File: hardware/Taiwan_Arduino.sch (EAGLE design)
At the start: 46 parts, among them J1 AVR_SPI_PRG_62X3_LOCK, T1 2SC, T2 2N, U1 ATMEGA328P_PDIP

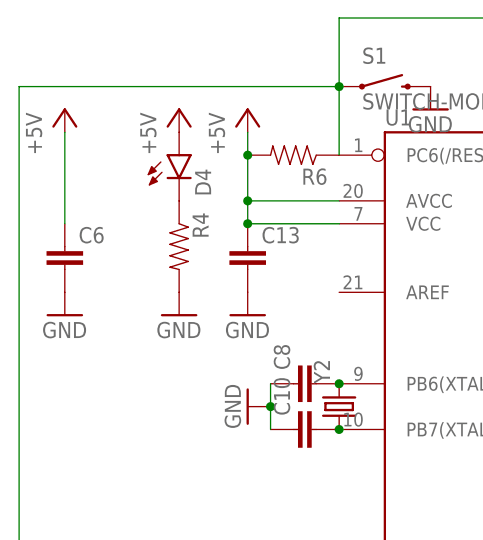
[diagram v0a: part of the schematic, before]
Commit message: Replaace bypass cap
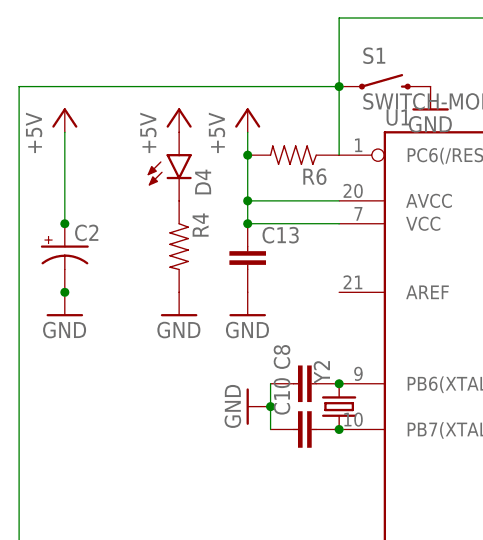
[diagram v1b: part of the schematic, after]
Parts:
- removed C6: (no value), SparkFun-Capacitors:CAPPTH1
- added C2: (no value), SparkFun-Capacitors:CAP_POLPTH1
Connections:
- net +5V: now also C2.+; no longer C6.1
- net GND: now also C2.-; no longer C6.2
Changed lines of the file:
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@@
 <grid distance="0.1" unitdist="inch" unit="inch" style="lines" multiple="1" display="no" altdistance="0.01" altunitdist="inch" altunit="inch"/>
 <layers>
-<layer number="1" name="Top" color="4" fill="1" visible="yes" active="no"/>
-<layer number="16" name="Bottom" color="1" fill="1" visible="yes" active="no"/>
-<layer number="17" name="Pads" color="2" fill="1" visible="yes" active="no"/>
-<layer number="18" name="Vias" color="2" fill="1" visible="yes" active="no"/>
-<layer number="19" name="Unrouted" color="6" fill="1" visible="yes" active="no"/>
-<layer number="20" name="Dimension" color="15" fill="1" visible="yes" active="no"/>
-<layer number="21" name="tPlace" color="7" fill="1" visible="yes" active="no"/>
-<layer number="22" name="bPlace" color="7" fill="1" visible="yes" active="no"/>
-<layer number="23" name="tOrigins" color="15" fill="1" visible="yes" active="no"/>
-<layer number="24" name="bOrigins" color="15" fill="1" visible="yes" active="no"/>
-<layer number="25" name="tNames" color="7" fill="1" visible="yes" active="no"/>
-<layer number="26" name="bNames" color="7" fill="1" visible="yes" active="no"/>
-<layer number="27" name="tValues" color="7" fill="1" visible="yes" active="no"/>
-<layer number="28" name="bValues" color="7" fill="1" visible="yes" active="no"/>
+<layer number="1" name="Top" color="4" fill="1" visible="no" active="no"/>
+<layer number="16" name="Bottom" color="1" fill="1" visible="no" active="no"/>
+<layer number="17" name="Pads" color="2" fill="1" visible="no" active="no"/>
+<layer number="18" name="Vias" color="2" fill="1" visible="no" active="no"/>
+<layer number="19" name="Unrouted" color="6" fill="1" visible="no" active="no"/>
+<layer number="20" name="Dimension" color="15" fill="1" visible="no" active="no"/>
+<layer number="21" name="tPlace" color="7" fill="1" visible="no" active="no"/>
+<layer number="22" name="bPlace" color="7" fill="1" visible="no" active="no"/>
+<layer number="23" name="tOrigins" color="15" fill="1" visible="no" active="no"/>
+<layer number="24" name="bOrigins" color="15" fill="1" visible="no" active="no"/>
+<layer number="25" name="tNames" color="7" fill="1" visible="no" active="no"/>
+<layer number="26" name="bNames" color="7" fill="1" visible="no" active="no"/>
+<layer number="27" name="tValues" color="7" fill="1" visible="no" active="no"/>
+<layer number="28" name="bValues" color="7" fill="1" visible="no" active="no"/>
 <layer number="29" name="tStop" color="7" fill="3" visible="no" active="no"/>
 <layer number="30" name="bStop" color="7" fill="6" visible="no" active="no"/>
@@
 <layer number="35" name="tGlue" color="7" fill="4" visible="no" active="no"/>
 <layer number="36" name="bGlue" color="7" fill="5" visible="no" active="no"/>
-<layer number="37" name="tTest" color="7" fill="1" visible="yes" active="no"/>
-<layer number="38" name="bTest" color="7" fill="1" visible="yes" active="no"/>
+<layer number="37" name="tTest" color="7" fill="1" visible="no" active="no"/>
+<layer number="38" name="bTest" color="7" fill="1" visible="no" active="no"/>
 <layer number="39" name="tKeepout" color="4" fill="11" visible="no" active="no"/>
 <layer number="40" name="bKeepout" color="1" fill="11" visible="no" active="no"/>
@@
 <layer number="44" name="Drills" color="7" fill="1" visible="no" active="no"/>
 <layer number="45" name="Holes" color="7" fill="1" visible="no" active="no"/>
-<layer number="46" name="Milling" color="3" fill="1" visible="yes" active="no"/>
-<layer number="47" name="Measures" color="7" fill="1" visible="yes" active="no"/>
-<layer number="48" name="Document" color="7" fill="1" visible="yes" active="no"/>
-<layer number="49" name="Reference" color="7" fill="1" visible="yes" active="no"/>
-<layer number="50" name="dxf" color="7" fill="1" visible="yes" active="no"/>
-<layer number="51" name="tDocu" color="7" fill="1" visible="yes" active="no"/>
-<layer number="52" name="bDocu" color="7" fill="1" visible="yes" active="no"/>
-<layer number="53" name="tGND_GNDA" color="7" fill="9" visible="yes" active="no"/>
-<layer number="54" name="bGND_GNDA" color="1" fill="9" visible="yes" active="no"/>
-<layer number="56" name="wert" color="7" fill="1" visible="yes" active="no"/>
-<layer number="57" name="tCAD" color="7" fill="1" visible="yes" active="no"/>
-<layer number="59" name="tCarbon" color="7" fill="1" visible="yes" active="no"/>
-<layer number="60" name="bCarbon" color="7" fill="1" visible="yes" active="no"/>
+<layer number="46" name="Milling" color="3" fill="1" visible="no" active="no"/>
+<layer number="47" name="Measures" color="7" fill="1" visible="no" active="no"/>
+<layer number="48" name="Document" color="7" fill="1" visible="no" active="no"/>
+<layer number="49" name="Reference" color="7" fill="1" visible="no" active="no"/>
+<layer number="50" name="dxf" color="7" fill="1" visible="no" active="no"/>
+<layer number="51" name="tDocu" color="7" fill="1" visible="no" active="no"/>
+<layer number="52" name="bDocu" color="7" fill="1" visible="no" active="no"/>
+<layer number="53" name="tGND_GNDA" color="7" fill="9" visible="no" active="no"/>
+<layer number="54" name="bGND_GNDA" color="1" fill="9" visible="no" active="no"/>
+<layer number="56" name="wert" color="7" fill="1" visible="no" active="no"/>
+<layer number="57" name="tCAD" color="7" fill="1" visible="no" active="no"/>
+<layer number="59" name="tCarbon" color="7" fill="1" visible="no" active="no"/>
+<layer number="60" name="bCarbon" color="7" fill="1" visible="no" active="no"/>
 <layer number="90" name="Modules" color="5" fill="1" visible="yes" active="yes"/>
 <layer number="91" name="Nets" color="2" fill="1" visible="yes" active="yes"/>
@@
 <part name="R17" library="SparkFun-Resistors" deviceset="RESISTOR" device="PTH-1/4W-VERT"/>
 <part name="P+8" library="supply1" deviceset="+5V" device=""/>
-<part name="C6" library="SparkFun-Capacitors" deviceset="CAP" device="PTH1"/>
 <part name="GND18" library="supply1" deviceset="GND" device=""/>
 <part name="T1" library="transistor" deviceset="2SC1815" device="" value="2SC"/>
 <part name="T2" library="adafruit" deviceset="2N2222" device="" value="2N"/>
+<part name="C2" library="SparkFun-Capacitors" deviceset="CAP_POL" device="PTH1"/>
 </parts>
 <sheets>
@@
 <instance part="R17" gate="G$1" x="109.22" y="86.36" rot="R270"/>
 <instance part="P+8" gate="1" x="7.62" y="137.16"/>
-<instance part="C6" gate="G$1" x="7.62" y="119.38"/>
 <instance part="GND18" gate="1" x="7.62" y="114.3"/>
 <instance part="T1" gate="G$1" x="160.02" y="83.82"/>
 <instance part="T2" gate="G$1" x="152.4" y="83.82"/>
+<instance part="C2" gate="G$1" x="7.62" y="121.92"/>
 </instances>
 <busses>
@@
 </segment>
 <segment>
-<pinref part="C6" gate="G$1" pin="2"/>
-<pinref part="GND18" gate="1" pin="GND"/>
-</segment>
-<segment>
 <pinref part="T1" gate="G$1" pin="E"/>
 <wire x1="154.94" y1="78.74" x2="162.56" y2="78.74" width="0.1524" layer="91"/>
@@
 <pinref part="T2" gate="G$1" pin="E"/>
 <junction x="162.56" y="78.74"/>
+</segment>
+<segment>
+<pinref part="GND18" gate="1" pin="GND"/>
+<pinref part="C2" gate="G$1" pin="-"/>
+<junction x="7.62" y="116.84"/>
+<pinref part="C2" gate="G$1" pin="-"/>
 </segment>
 </net>
@@
 </segment>
 <segment>
-<pinref part="C6" gate="G$1" pin="1"/>
 <wire x1="7.62" y1="134.62" x2="7.62" y2="124.46" width="0.1524" layer="91"/>
 <pinref part="P+8" gate="1" pin="+5V"/>
-</segment>
-<segment>
+<pinref part="C2" gate="G$1" pin="+"/>
+<junction x="7.62" y="124.46"/>
+</segment>
+<segment>

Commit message: Layout fixed
1.reduce via under the 328p mcu
2.fix the reset pin routing of the isp header
3.beef up the power/ground wires near C13 / reset button and USB shell
4.rotate the speaker header and transistors 45 deg
5.make more space for capacitor C1/C2
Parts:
- removed C3: (no value), SparkFun-Capacitors:CAPPTH1
- added C1: (no value), adafruit:CPOL-USE2.5-5
- C2: device SparkFun-Capacitors:CAP_POLPTH1 -> adafruit:CPOL-USE5-10.5
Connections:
- removed net N$30: C3.2, JP3.2
- net +5V: now also C1.+
- net GND: now also C1.-
- net N$18: now also JP3.2; no longer C3.1
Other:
- moved on the sheet: C2

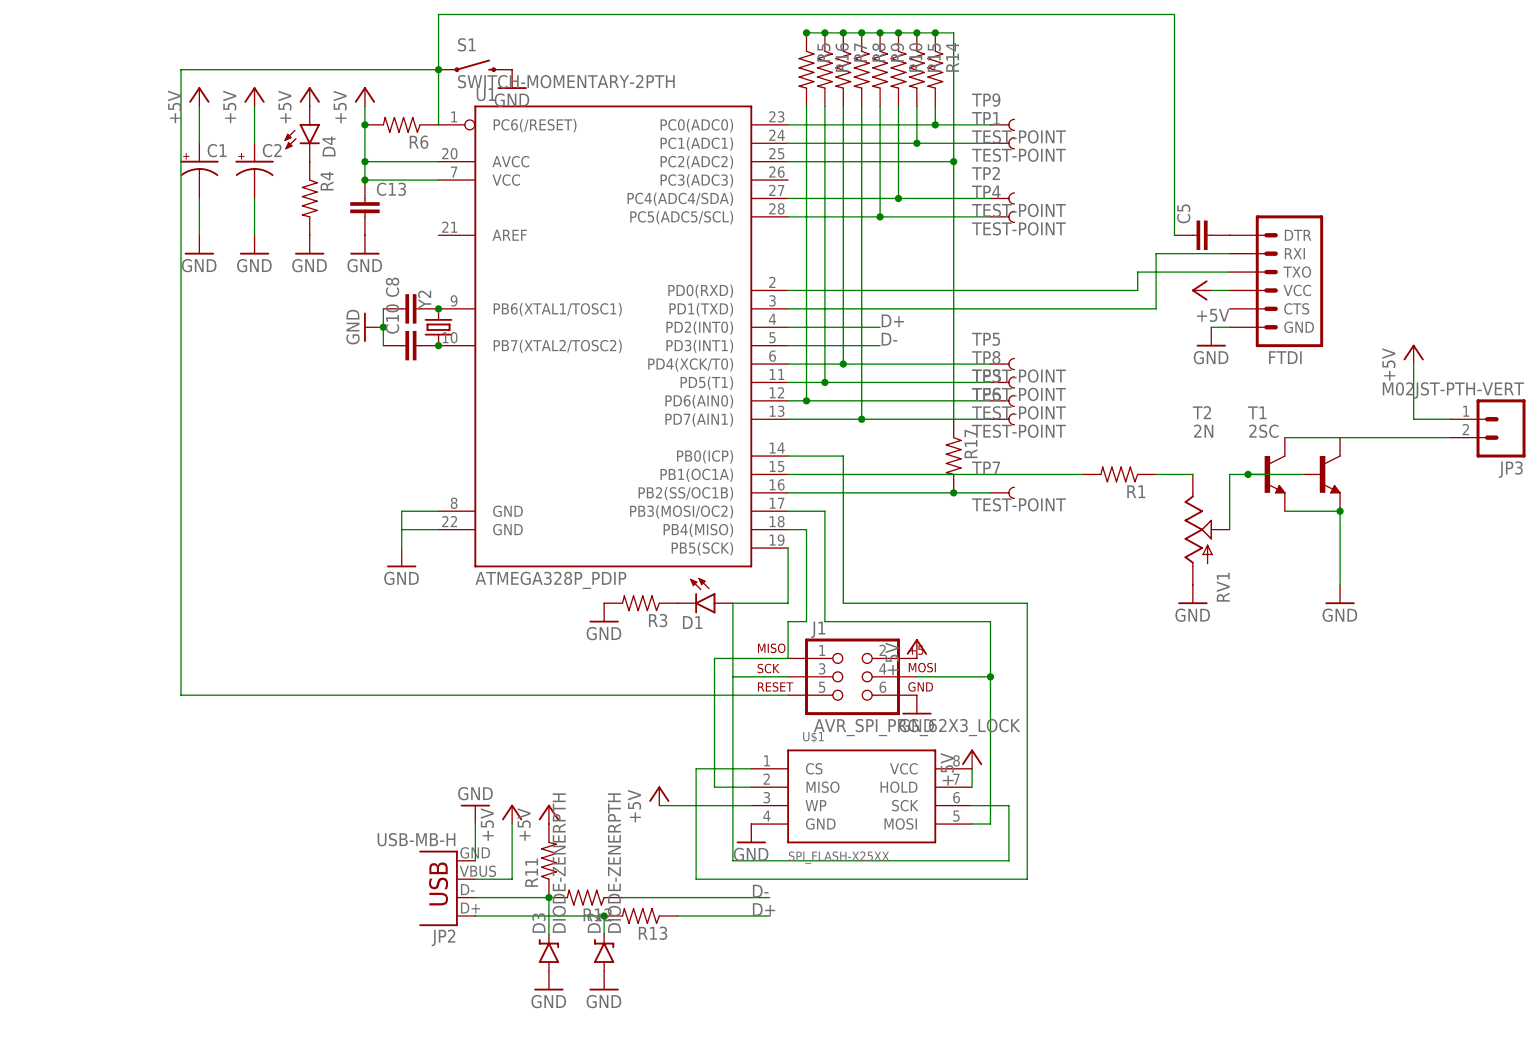
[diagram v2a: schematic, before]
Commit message: Improve touch pad grounding
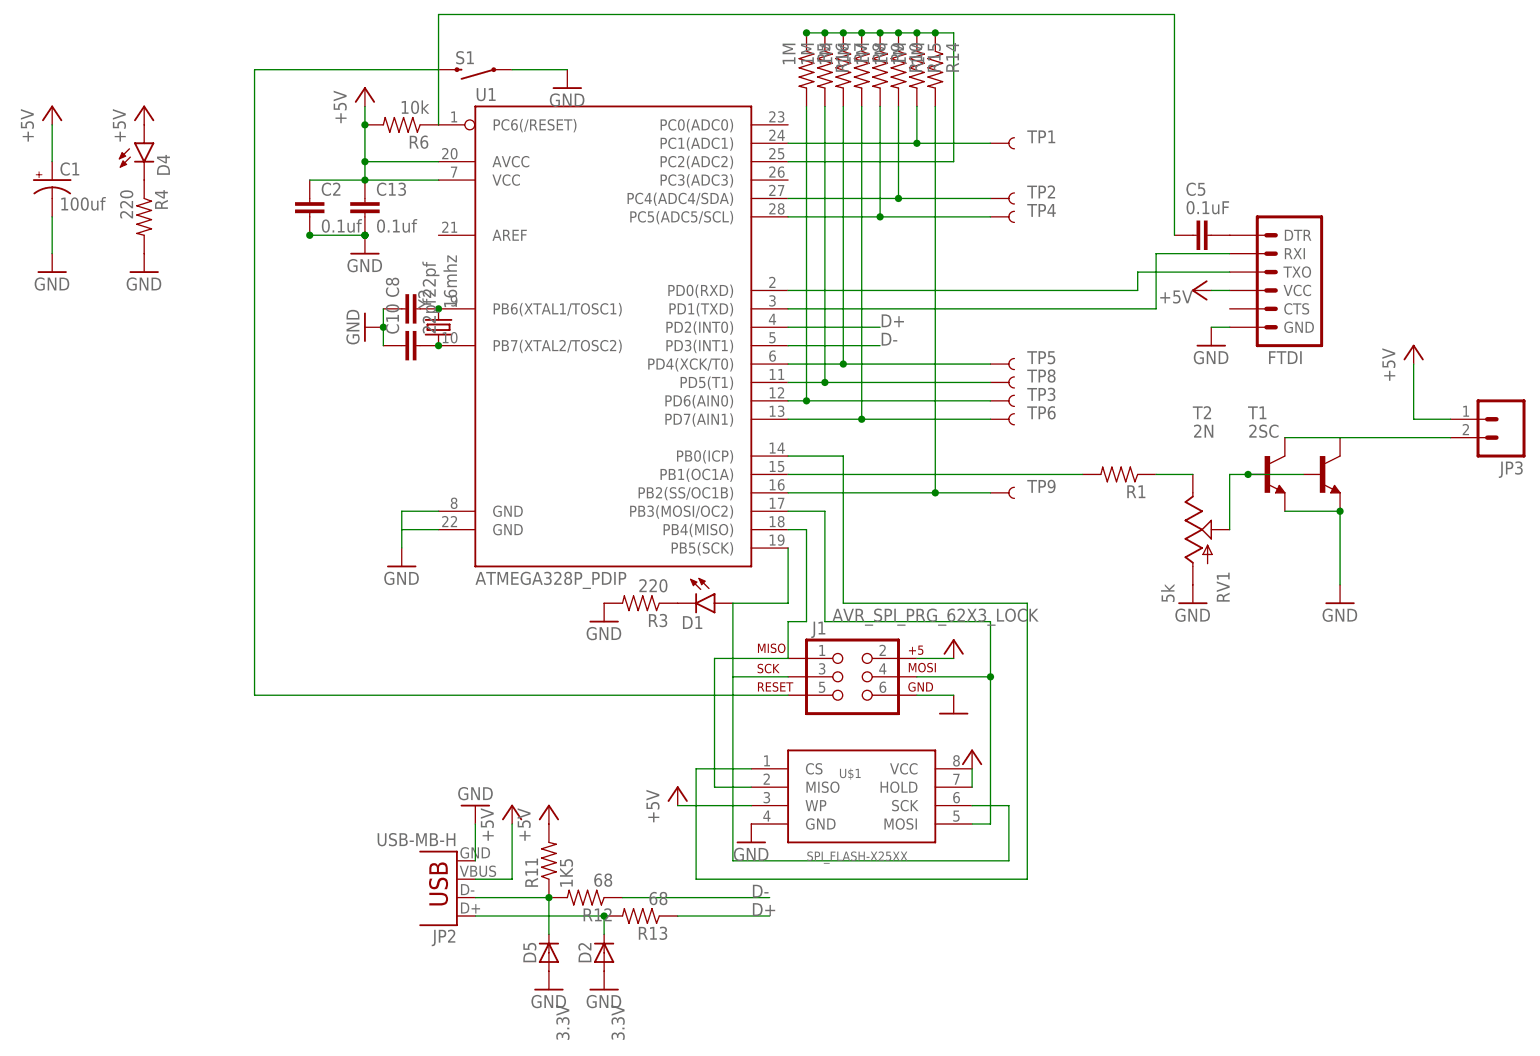
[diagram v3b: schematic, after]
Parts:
- removed D3: DIODE-ZENERPTH, SparkFun-DiscreteSemi:DIODE-ZENERPTH
- removed R17: (no value), SparkFun-Resistors:RESISTORPTH-1/4W-VERT
- removed TP7: TEST-POINT, SparkFun-Passives:TEST-POINT
- added D5: 3.3V, _JJG-parts:DIODE-VERTDIODE_SM_VERT
- C1: value (none) -> 100uf
- C10, C8: value (none) -> 22pf
- C13: value (none) -> 0.1uf
- C2: value (none) -> 0.1uf; device adafruit:CPOL-USE5-10.5 -> SparkFun-Capacitors:CAPPTH
- C5: value (none) -> 0.1uF
- D2: value DIODE-ZENERPTH -> 3.3V; device SparkFun-DiscreteSemi:DIODE-ZENERPTH -> _JJG-parts:DIODE-VERTDIODE_SM_VERT
- R1: device SparkFun-Resistors:RESISTORPTH-1/4W-VERT -> SparkFun-Resistors:RESISTORPTH-1/4W
- R10, R15, R16, R5, R7, R8, R9: value (none) -> 1M
- R11: value (none) -> 1K5
- R12, R13: value (none) -> 68
- R14: value (none) -> 1M; device SparkFun-Resistors:RESISTORPTH-1/4W-VERT -> SparkFun-Resistors:RESISTORPTH-1/4W
- R3, R4: value (none) -> 220
- R6: value (none) -> 10k
- RV1: value (none) -> 5k
- Y2: value (none) -> 16mhz
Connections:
- removed net N$12: R17.2, TP7.1, U1.PB2(SS/OC1B)
- net +5V: now also C2.1; no longer C2.+
- net GND: now also C2.2, D5.A, S1.1; no longer C2.-, D3.A, S1.2
- net N$11: no longer R17.1
- net N$15: now also D5.C; no longer D3.C
- net N$3: now also U1.PB2(SS/OC1B); no longer U1.PC0(ADC0)
- net RST: now also S1.2; no longer S1.1
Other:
- moved on the sheet: C1, D4, R4, S1, TP9
